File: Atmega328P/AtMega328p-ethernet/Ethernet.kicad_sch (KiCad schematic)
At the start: 20 parts, among them J3 RJ45_Abracon_ARJP11A-MASA-B-A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, U2 W5500

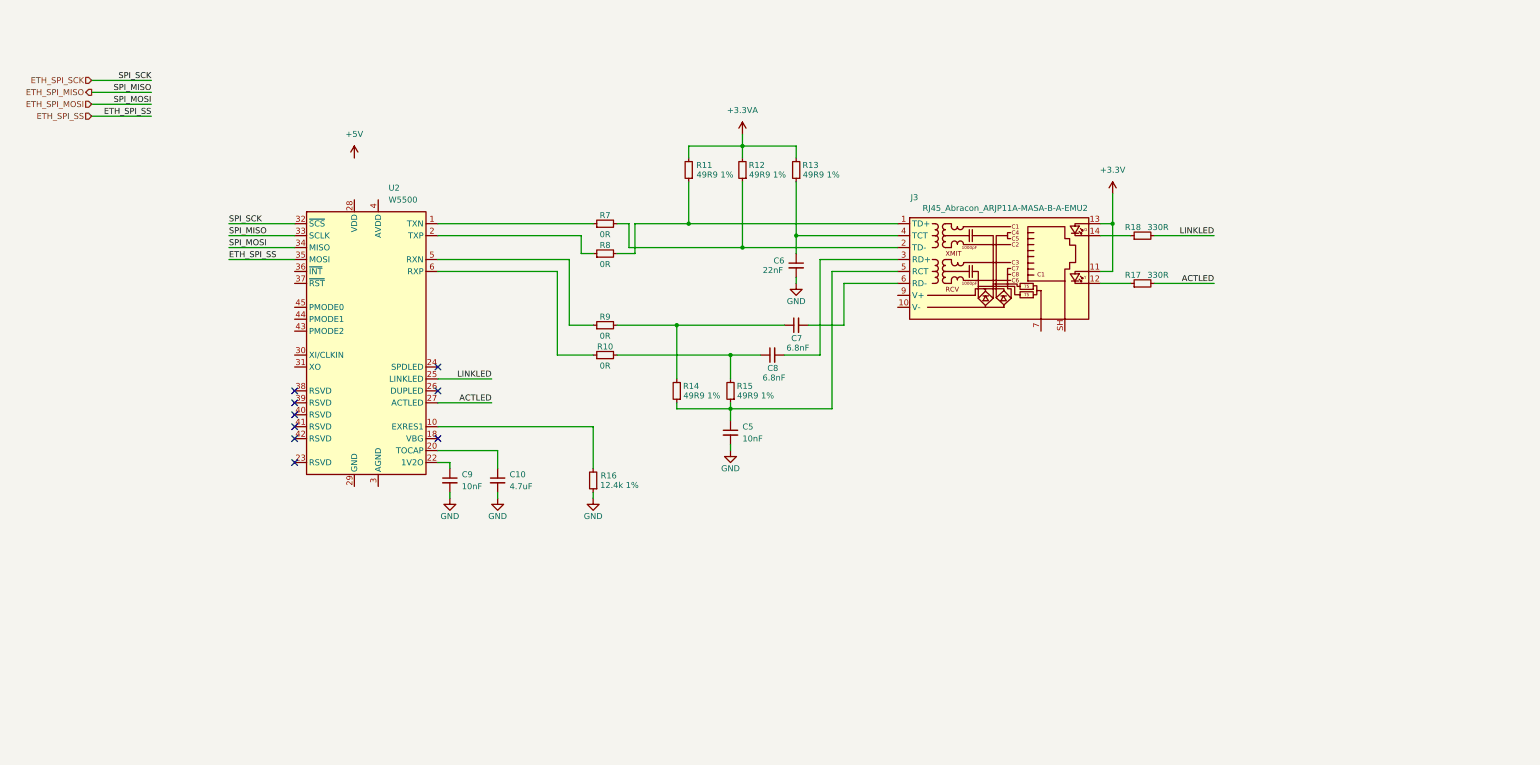
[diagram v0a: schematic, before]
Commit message: Most main components layed out
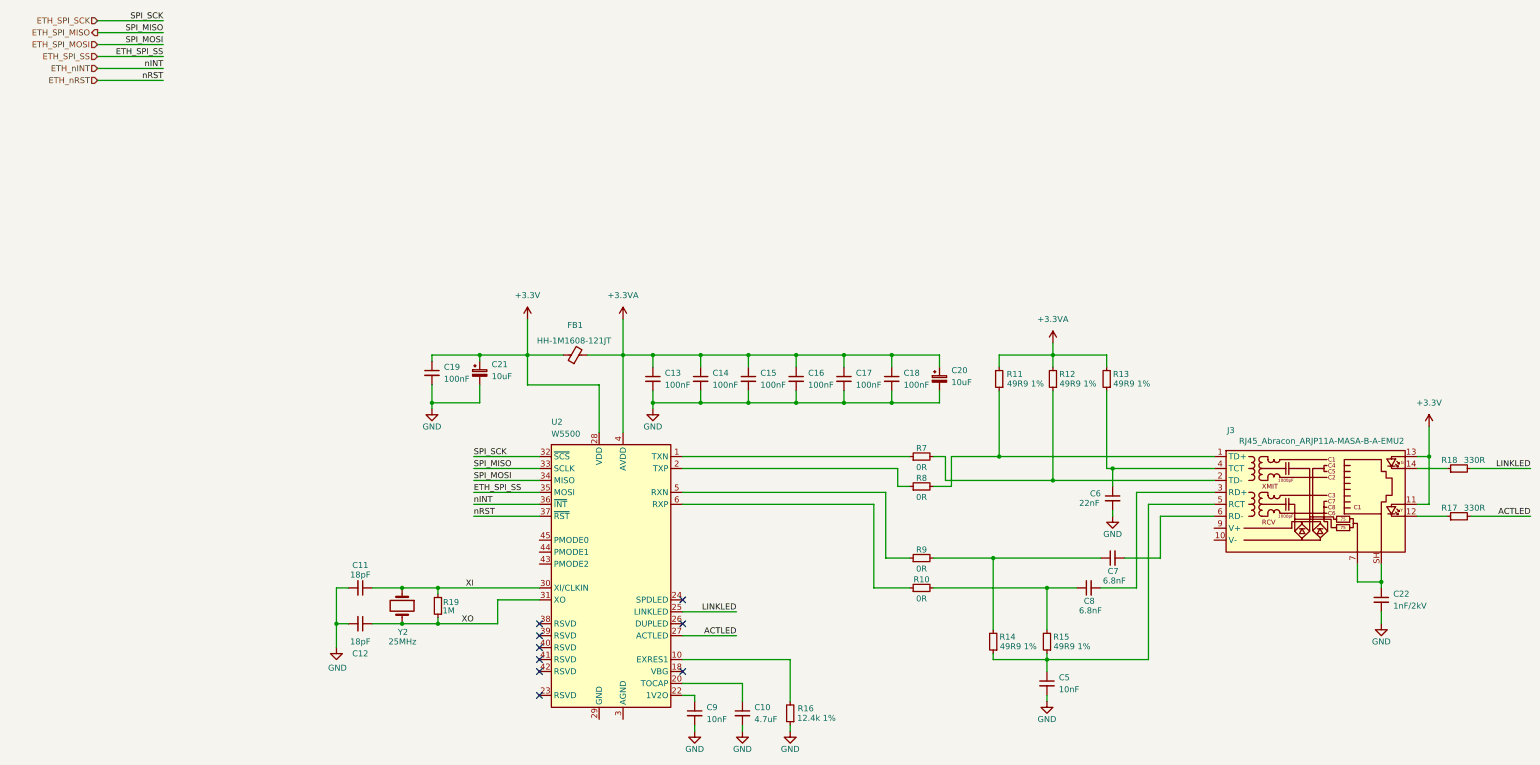
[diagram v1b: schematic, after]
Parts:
- added C11, C12: 18pF, symbol Device:C_Small
- added C13, C14, C15, C16, C17, C18, C19: 100nF, symbol Device:C_Small
- added C20, C21: 10uF, symbol Device:C_Polarized_Small
- added C22: 1nF/2kV, symbol Device:C_Small
- added FB1: HH-1M1608-121JT, symbol Device:FerriteBead_Small
- added R19: 1M, symbol Device:R_Small
- added Y2: 25MHz, symbol Device:Crystal
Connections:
- net +3.3V: now also U2.28 (VDD), C19.1, C21.1, FB1.1
- net +3.3VA: now also U2.11 (AVDD), U2.15 (AVDD), U2.17 (AVDD), U2.21 (AVDD), U2.4 (AVDD), U2.8 (AVDD), C13.1, C14.1, C15.1, C16.1, C17.1, C18.1, C20.1, FB1.2
- net GND: now also C11.2, C12.2, C13.2, C14.2, C15.2, C16.2, C17.2, C18.2, C19.2, C20.2, C21.2, C22.2
- net XI: now reaches U2.30 (XI/CLKIN)
- net XI: now also C11.1, R19.2, Y2.1
- net XO: now reaches U2.31 (XO)
- net XO: now also C12.1, R19.1, Y2.2
- net ETH_nINT: now reaches U2.36 (~{INT})
- net ETH_nRST: now reaches U2.37 (~{RST})
- net at J3.7: now also J3.SH, C22.1
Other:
- moved on the sheet: C10, C5, C6, C7, C8, C9, J3, R10, R11, R12, R13, R14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

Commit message: Schematic draft complete
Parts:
- C10, C20, C21: footprint (none) -> Capacitor_SMD:CP_Elec_4x3
- C11, C12, C13, C14, C15, C16, C17, C18, C19, C22, C5, C6, C7, C8, C9: footprint (none) -> Capacitor_SMD:C_0603_1608Metric
- FB1: footprint (none) -> Inductor_SMD:L_0603_1608Metric
- R10, R11, R12, R13, R14, R15, R16, R17, R18, R19, R7, R8, R9: footprint (none) -> Resistor_SMD:R_0603_1608Metric
- Y2: footprint (none) -> Crystal:Crystal_SMD_2012-2Pin_2.0x1.2mm
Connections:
- no-connect marks 9 -> 11
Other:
- company: (none) -> HUNTER INC.
- title: (none) -> ETHERNET INTERFACE

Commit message: PCB Layout done initial
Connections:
- net ETH_RXP_C: now reaches C8.2, J3.3 (RD+)
- net ETH_RXN_C: now reaches C7.2, J3.6 (RD-)
- net ETH_RXN: now reaches R9.1, U2.5 (RXN)
- net ETH_TXN: now reaches R7.1, U2.1 (TXN)
- net ETH_TXP: now reaches R8.1, U2.2 (TXP)
- net ETH_RXP: now reaches R10.1, U2.6 (RXP)
- net ETH_TXN_C: now reaches J3.2 (TD-), R12.1, R7.2
- net ETH_TXP_C: now reaches J3.1 (TD+), R11.1, R8.2
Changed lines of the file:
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@@
+		)
+	)
+	(label "ETH_TXP_C"
+		(at 275.59 118.11 180)
+		(effects
+			(font
+				(size 1.27 1.27)
+			)
+			(justify right bottom)
 		)
 	)
@@
 		)
 	)
+	(label "ETH_TXP"
+		(at 177.8 120.65 180)
+		(effects
+			(font
+				(size 1.27 1.27)
+			)
+			(justify right bottom)
+		)
+	)
 	(label "ETH_SPI_SS"
 		(at 63.5 40.64 180)
+		(effects
+			(font
+				(size 1.27 1.27)
+			)
+			(justify right bottom)
+		)
+	)
+	(label "ETH_RXN_C"
+		(at 275.59 130.81 180)
 		(effects
 			(font
@@
 		)
 	)
+	(label "ETH_RXN"
+		(at 177.8 125.73 180)
+		(effects
+			(font
+				(size 1.27 1.27)
+			)
+			(justify right bottom)
+		)
+	)
+	(label "ETH_TXN"
+		(at 177.8 118.11 180)
+		(effects
+			(font
+				(size 1.27 1.27)
+			)
+			(justify right bottom)
+		)
+	)
 	(label "XI"
 		(at 119.38 146.05 180)
+		(effects
+			(font
+				(size 1.27 1.27)
+			)
+			(justify right bottom)
+		)
+	)
+	(label "ETH_RXP"
+		(at 177.8 128.27 180)
 		(effects
 			(font
@@
 			)
 			(justify left bottom)
+		)
+	)
+	(label "ETH_RXP_C"
+		(at 275.59 125.73 180)
+		(effects
+			(font
+				(size 1.27 1.27)
+			)
+			(justify right bottom)
 		)
 	)
@@
 		(effects
 			(font
+				(size 1.27 1.27)
+			)
+			(justify right bottom)
+		)
+	)
+	(label "ETH_TXN_C"
+		(at 275.59 123.19 180)
+		(effects
+			(font
